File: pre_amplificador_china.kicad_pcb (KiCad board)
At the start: 2 copper layers, 106.7 x 51.2 mm, 84 parts, among them J1 Conn_01x02, J2 Conn_01x02, J202 Conn_01x04, J3 Conn_01x03, J4 Conn_01x03, K301 ADW11, Q2 BSS138, Q301 BSS138, Q302 BSS138, SW1 SW_Push_Dual, U1 TL072, U106 LM7805_TO220, U2 TL074, U202 HT66F0175_185

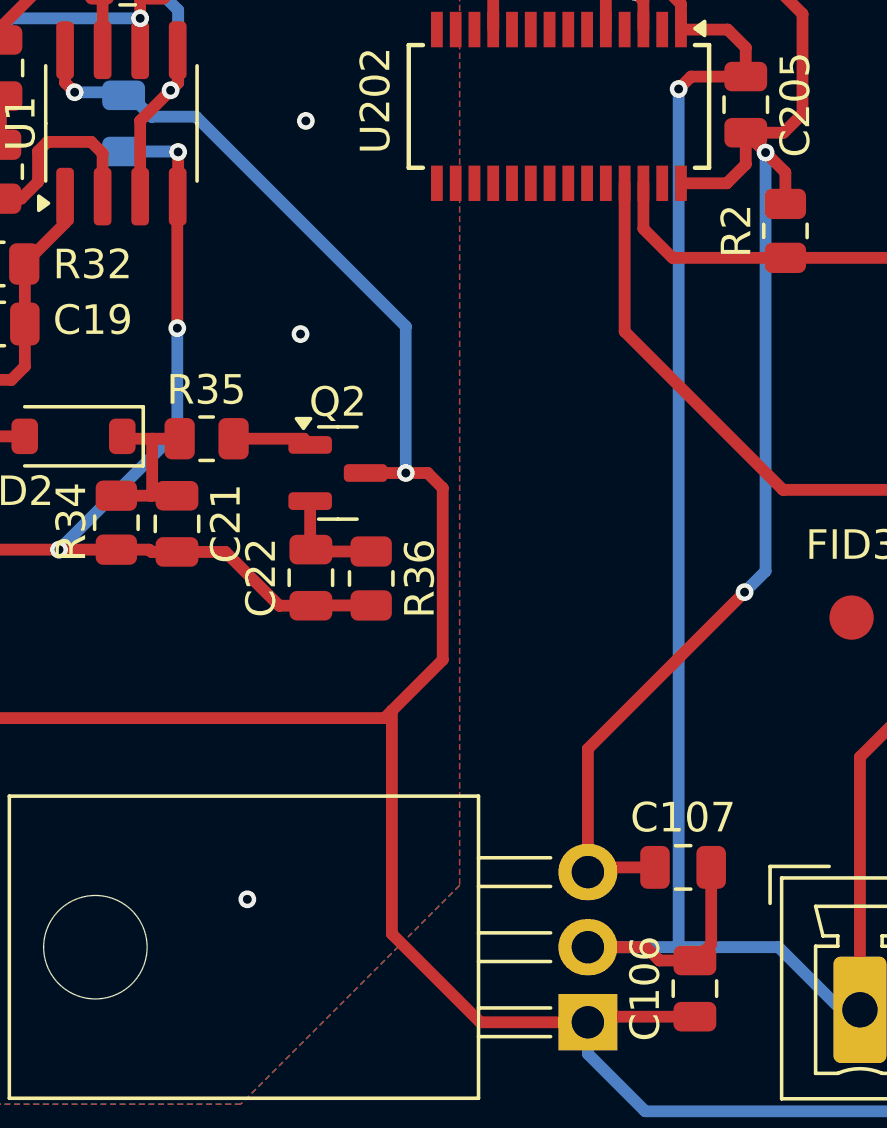
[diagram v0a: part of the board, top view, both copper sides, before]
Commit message: correcao de standby no IC
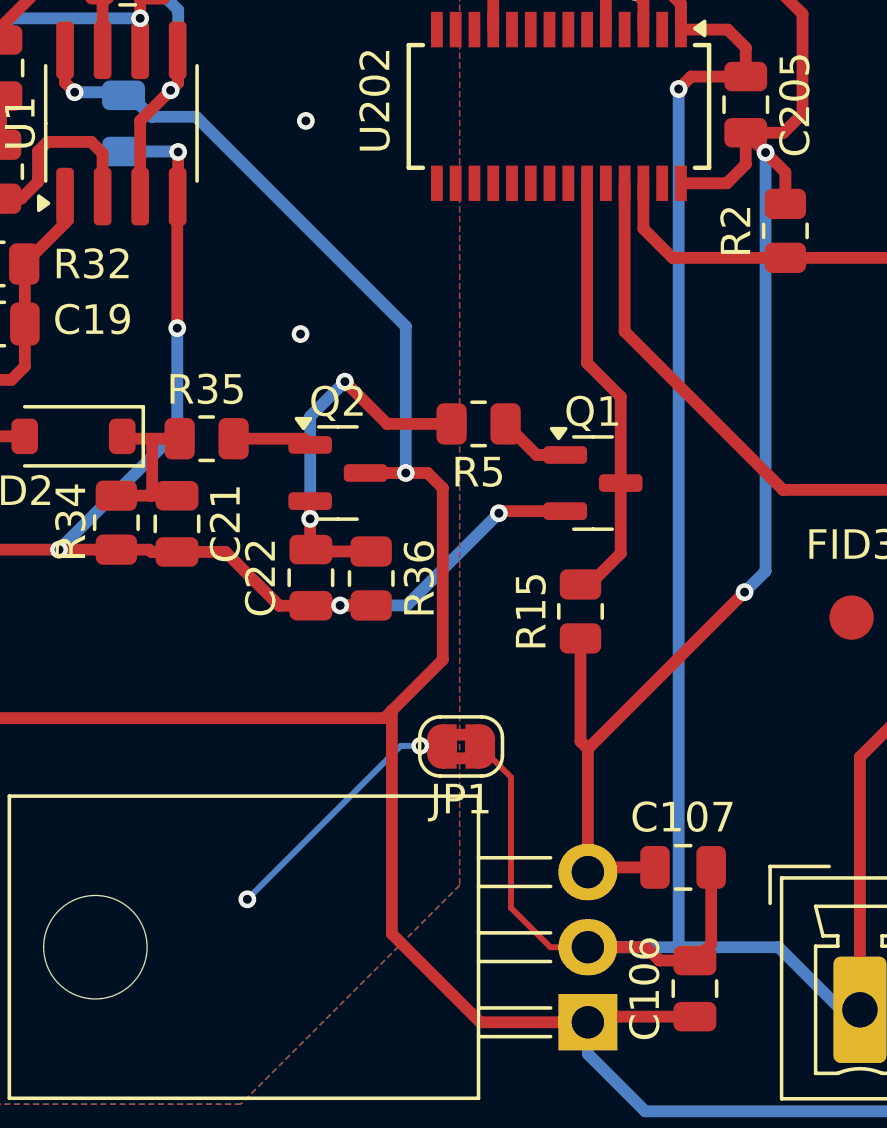
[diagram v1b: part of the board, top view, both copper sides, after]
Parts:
- added JP1: SolderJumper_2_Bridged, Jumper:SolderJumper-2_P1.3mm_Bridged2Bar_RoundedPad1.0x1.5mm, F.Cu at (146.7, 103.8)
- added Q1: BSS138, Package_TO_SOT_SMD:SOT-23, F.Cu at (151.1, 94.9)
- added R15: 10k, Resistor_SMD:R_0805_2012Metric, F.Cu at (150.7, 99.2)
- added R5: 1k, Resistor_SMD:R_0805_2012Metric, F.Cu at (147.3, 92.9)
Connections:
- U202 pad 23: unconnected-(U202-PD3/SSEG14-Pad23) -> ST_LOW
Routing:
- net GND1: track 113.4 -> 131.1 mm, vias 21 -> 24
- net ST_LOW: track 0.00 -> 14.8 mm
- net ST: track 3.72 -> 13.0 mm, vias 0 -> 2
- net VSS: track 106.5 -> 115.6 mm
- net VDD: track 48.6 -> 52.4 mm
- net Net-(Q1-G): track 0.00 -> 2.45 mm

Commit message: v2.0 pre APL_STA2150
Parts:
- removed D1: LED, LED_THT:LED_D3.0mm_Clear
- removed H4: MountingHole, MountingHole:MountingHole_3.5mm
- removed J3: Conn_01x03, Connector_JST:JST_XH_B3B-XH-A_1x03_P2.50mm_Vertical
- removed R10, R6, R7, R8, R9: 100k, Resistor_SMD:R_0805_2012Metric
- added C10: 100nf, Capacitor_SMD:C_0805_2012Metric, F.Cu at (126.2, 107.2)
- added C25: 100nf, Capacitor_SMD:C_0805_2012Metric, F.Cu at (105.4, 81.2)
- added C27: 100nf, Capacitor_SMD:C_0805_2012Metric, F.Cu at (139.2, 81.2)
- added C28: 100nf, Capacitor_SMD:C_0805_2012Metric, F.Cu at (137.6, 87.9)
- added C8: 2.2uF, Capacitor_SMD:C_0805_2012Metric, B.Cu at (135.2, 82.8)
- added C9: 2.2uF, Capacitor_SMD:C_0805_2012Metric, B.Cu at (124.8, 102.1)
- added J5: Conn_01x03, Connector_JST:JST_XH_B3B-XH-A_1x03_P2.50mm_Vertical, F.Cu at (100.4, 106.4)
- added J6: Conn_01x04, Connector_JST:JST_XH_B4B-XH-A_1x04_P2.50mm_Vertical, F.Cu at (111.5, 101.4)
- added J7: Conn_01x04, Connector_JST:JST_XH_B4B-XH-A_1x04_P2.50mm_Vertical, F.Cu at (100.7, 112.8)
- added U3: TL072, Package_SO:SOIC-8_3.9x4.9mm_P1.27mm, F.Cu at (124.8, 102.1)
- C11, C12, C24: moved to F.Cu
- C13: value 2.2uF -> 100nf
- C14, C15: value 470pF -> 33pF
- C22: value 10uF -> X
- C23: value 10uF -> 2.2uF
- J4: value Conn_01x03 -> Conn_01x01; footprint Connector_JST:JST_XH_B3B-XH-A_1x03_P2.50mm_Vertical -> Connector_PinHeader_2.54mm:PinHeader_1x01_P2.54mm_Vertical
- R19, R21: value 100k -> 10k
- R22, R24: value 1k -> 10k; moved to F.Cu
- R23, R25, R31: value 1k -> 100k
- R3: value 100k -> 10
- R32: value 1k -> 10k
- R34: value 570k -> 10k
- SW1: value SW_Push_Dual -> SW_Push; footprint Library:ButtonLoud -> Library:Button
- moved R21 37.8 mm to (126.0, 112.8)
- moved R19 37.8 mm to (122.5, 112.8)
- moved R20 33.2 mm to (125.1, 110.0), turned to 90 degrees
- moved FID3 31.4 mm to (149.7, 69.8)
- moved C24 30.5 mm to (121.5, 110.0), turned to 90 degrees
- moved R3 29.9 mm to (139.3, 102.0), turned to 180 degrees
- moved R301 26.4 mm to (191.1, 81.4)
- moved Q301 26.4 mm to (193.1, 78.2)
- moved Q302 26.4 mm to (186.3, 80.3)
- moved R302 26.4 mm to (186.4, 84.2)
- moved R307 26.4 mm to (187.2, 76.5)
- moved R205 18.8 mm to (149.7, 90.0), turned to 180 degrees
- moved C13 17.1 mm to (105.0, 93.1), turned to -90 degrees
- moved FID4 15.1 mm to (96.5, 99.6)
- moved J1 13.3 mm to (174.6, 112.8)
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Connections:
- C1 pad 1: Net-(C1-Pad1) -> BT_R
- C1 pad 2: BT_R -> Net-(C1-Pad2)
- C11 pad 1: Net-(C1-Pad1) -> Net-(C1-Pad2)
- C13 pad 1: Net-(C13-Pad1) -> V/2_AUDIO
- C23 pad 1: +12V -> GND1
- C23 pad 2: GND1 -> Net-(U1C-V+)
- C24 pad 1: +12V -> Net-(U1C-V+)
- C5 pad 1: +12V -> Net-(U1C-V+)
- J4 pad 1: BT_R -> ST_OUT
- K301 pad 3: Net-(J1-Pin_1) -> Net-(J1-Pin_2)
- K301 pad 5: Net-(J1-Pin_2) -> Net-(J1-Pin_1)
- R13 pad 1: Net-(C1-Pad1) -> Net-(C1-Pad2)
- R19 pad 1: +12V -> Net-(U1C-V+)
- R19 pad 2: Net-(C13-Pad1) -> Net-(R19-Pad2)
- R20 pad 1: Net-(C13-Pad1) -> Net-(R19-Pad2)
- R20 pad 2: V/2 -> Net-(U3A-+)
- R205 pad 2: Net-(D1-A) -> ST_OUT
- R21 pad 1: Net-(C13-Pad1) -> Net-(R19-Pad2)
- R3 pad 1: +12V -> VDD
- R3 pad 2: Net-(R3-Pad2) -> Net-(U1C-V+)
- SW1 pad 2: unconnected-(SW1-Pad2) -> VSS
- U1 pad 8: +12V -> Net-(U1C-V+)
- U2 pad 3: Net-(U2A-+) -> V/2_AUDIO
- U2 pad 4: +12V -> Net-(U1C-V+)
- U2 pad 5: Net-(U2B-+) -> V/2_AUDIO
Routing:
- net Net-(U1C-V+): track 0.00 -> 94.0 mm, vias 0 -> 7
- net +12V: track 187.7 -> 103.5 mm, vias 6 -> 2
- net GND1: track 131.1 -> 56.1 mm
- net ST_OUT: track 0.00 -> 60.2 mm, vias 0 -> 2
- net V/2_AUDIO: track 0.00 -> 40.0 mm, vias 0 -> 2
- net V/2: track 46.2 -> 65.9 mm, vias 2 -> 4
- net Net-(J1-Pin_1): track 10.9 -> 24.6 mm
- net RELE: track 26.6 -> 39.8 mm, vias 0 -> 2
- net Net-(U2B--): track 20.2 -> 7.92 mm
- net VDD: track 52.4 -> 62.4 mm
- net Net-(D301-A): track 26.6 -> 17.4 mm
- net Net-(U202-PB1/INT1/SSEG17/AN1/XT2): track 22.4 -> 30.5 mm, vias 0 -> 2
- net Net-(J1-Pin_2): track 14.2 -> 6.79 mm
- net Net-(J5-Pin_3): track 3.81 -> 11.0 mm
- net Net-(J5-Pin_1): track 3.78 -> 10.9 mm
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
